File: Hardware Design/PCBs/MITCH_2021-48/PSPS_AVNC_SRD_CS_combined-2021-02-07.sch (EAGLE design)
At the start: 1 part, among them U0-C STM32F411CEUX

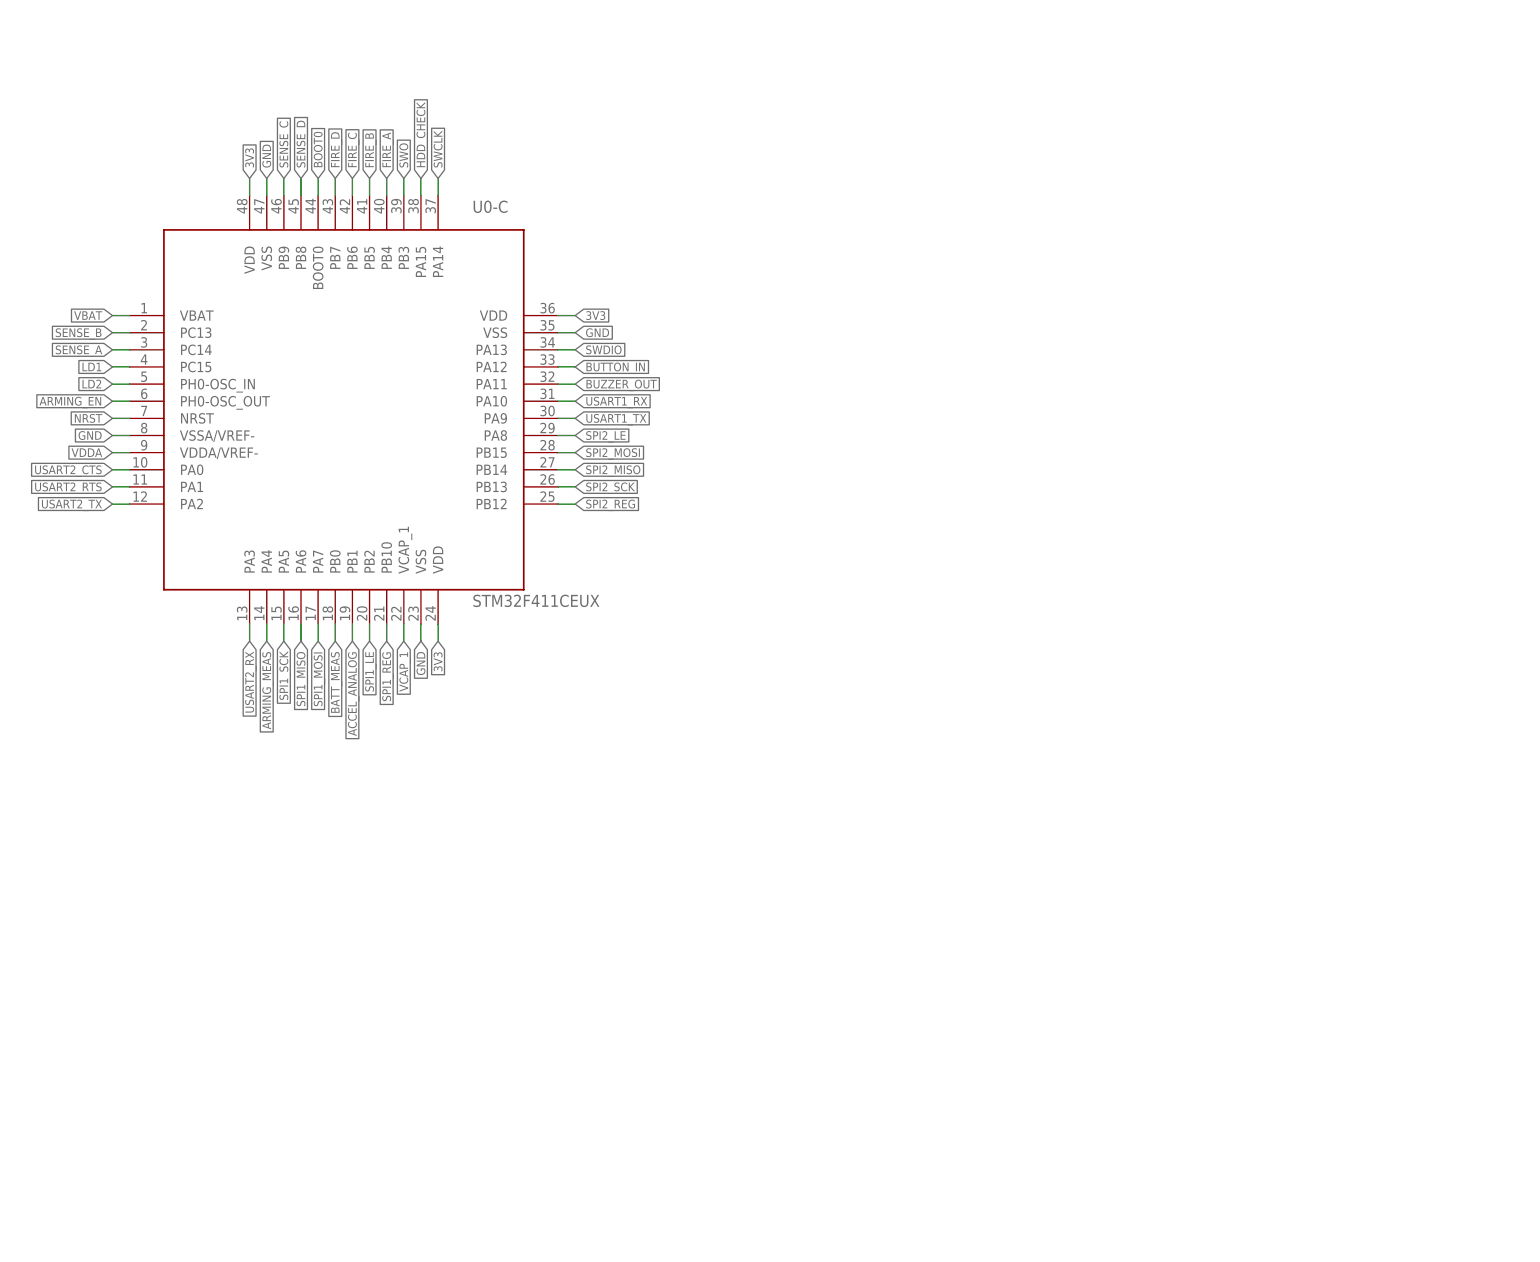
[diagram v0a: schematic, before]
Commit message: Added Shift Registeres, Split Octal Buffers
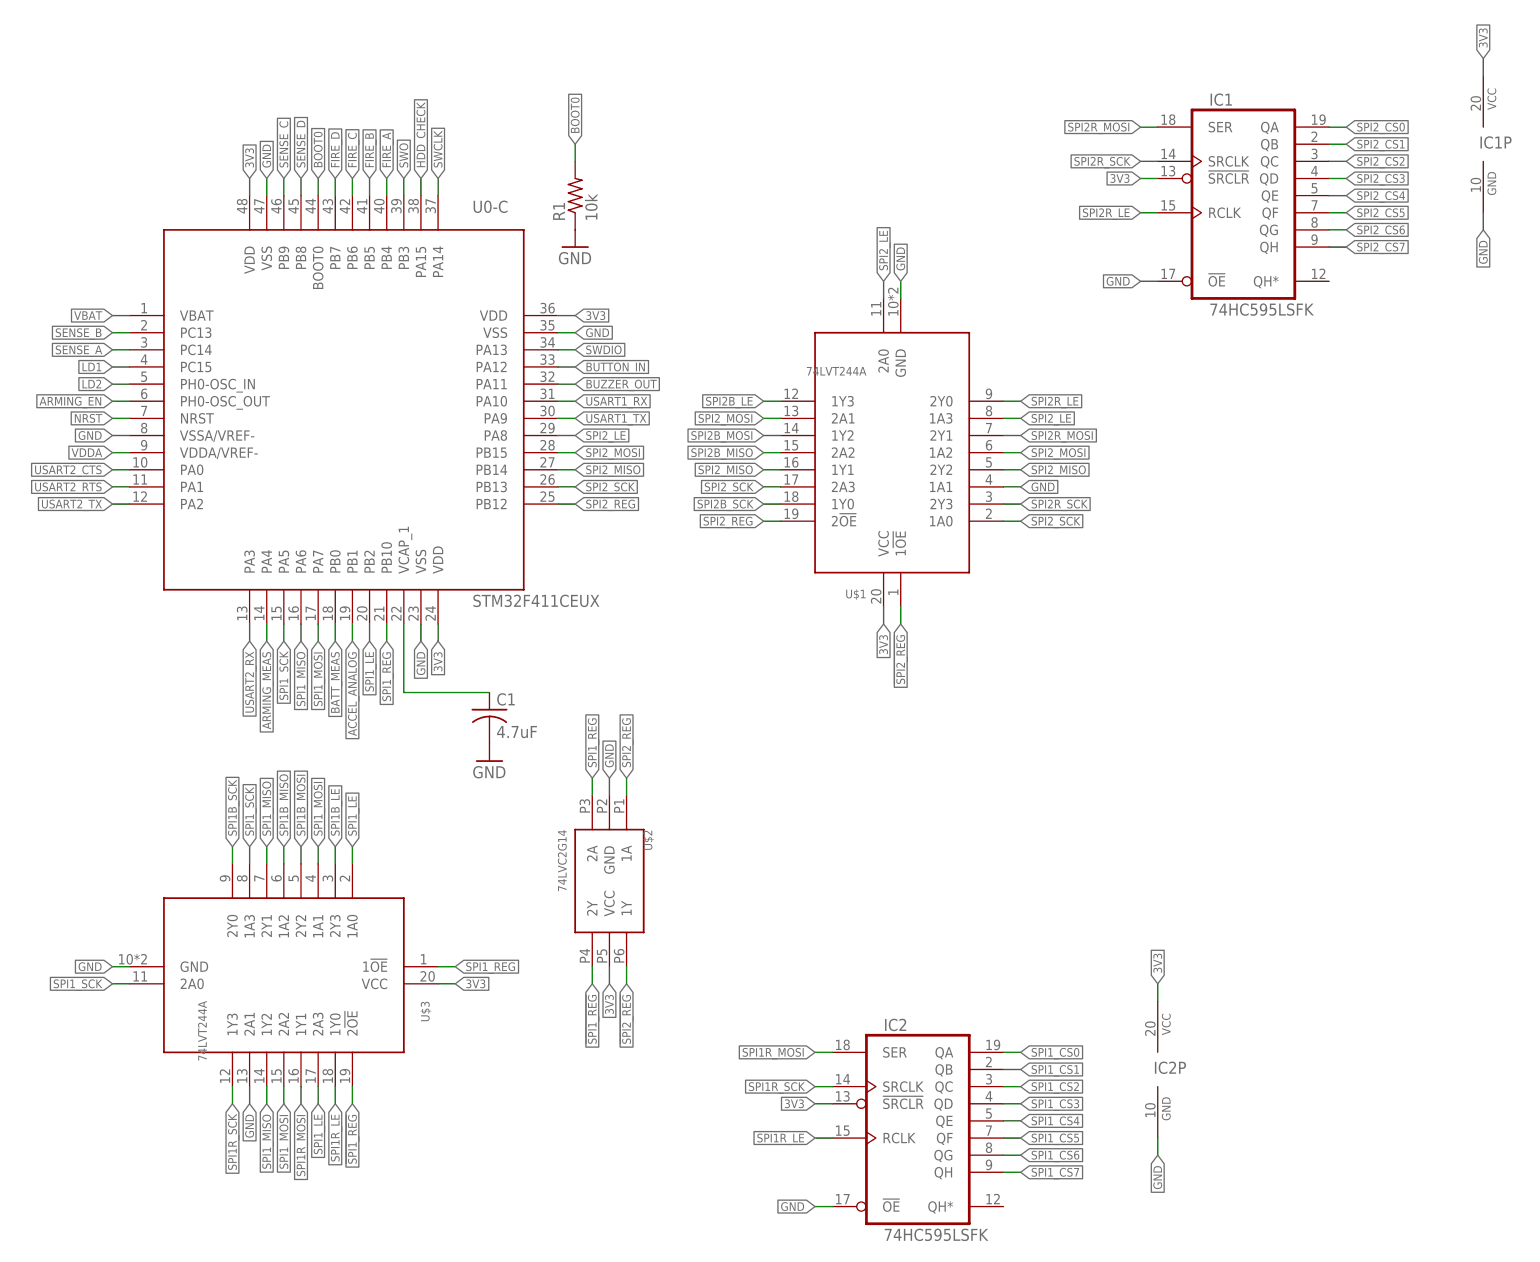
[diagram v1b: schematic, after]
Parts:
- added C1: 4.7uF, resistor:C-USC0805
- added IC1, IC2: 74HC595LSFK, Computer2:74HC595LSFK
- added R1: 10k, resistor:R-US_M0805
- added U$1, U$3: 74LVT244A, Computer2:74LVT244A
- added U$2: 74LVC2G14, Computer2:74LVC2G14
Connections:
- new net !SPI1_REG!: U$2.2Y, U$3.2!OE!
- new net !SPI2_REG!: U$1.1!OE!, U$2.1Y
- new net SPI1B_LE: U$3.2Y3
- new net SPI1B_MISO: U$3.1A2
- new net SPI1B_MOSI: U$3.2Y2
- new net SPI1B_SCK: U$3.2Y0
- new net SPI1R_LE: IC2G$1.RCLK, U$3.1Y0
- new net SPI1R_MOSI: IC2G$1.SER, U$3.1Y1
- new net SPI1R_SCK: IC2G$1.SRCLK, U$3.1Y3
- new net SPI1_CS0: IC2G$1.QA
- new net SPI1_CS1: IC2G$1.QB
- new net SPI1_CS2: IC2G$1.QC
- new net SPI1_CS3: IC2G$1.QD
- new net SPI1_CS4: IC2G$1.QE
- new net SPI1_CS5: IC2G$1.QF
- new net SPI1_CS6: IC2G$1.QG
- new net SPI1_CS7: IC2G$1.QH
- new net SPI2B_LE: U$1.1Y3
- new net SPI2B_MISO: U$1.2A2
- new net SPI2B_MOSI: U$1.1Y2
- new net SPI2B_SCK: U$1.1Y0
- new net SPI2R_LE: IC1G$1.RCLK, U$1.2Y0
- new net SPI2R_MOSI: IC1G$1.SER, U$1.2Y1
- new net SPI2R_SCK: IC1G$1.SRCLK, U$1.2Y3
- new net SPI2_CS0: IC1G$1.QA
- new net SPI2_CS1: IC1G$1.QB
- new net SPI2_CS2: IC1G$1.QC
- new net SPI2_CS3: IC1G$1.QD
- new net SPI2_CS4: IC1G$1.QE
- new net SPI2_CS5: IC1G$1.QF
- new net SPI2_CS6: IC1G$1.QG
- new net SPI2_CS7: IC1G$1.QH
- net 3V3: now also IC1G$1.!SRCLR!, IC1P.VCC, IC2G$1.!SRCLR!, IC2P.VCC, U$1.VCC, U$2.VCC, U$3.VCC
- net BOOT0: now also R1.2
- net GND: now also C1.2, IC1G$1.!OE!, IC1P.GND, IC2G$1.!OE!, IC2P.GND, R1.1, U$1.1A1, U$1.GND, U$2.GND, U$3.2A1, U$3.GND
- net SPI1_LE: now also U$3.1A0, U$3.2A3
- net SPI1_MISO: now also U$3.1Y2, U$3.2Y1
- net SPI1_MOSI: now also U$3.1A1, U$3.2A2
- net SPI1_REG: now also U$2.2A, U$3.1!OE!
- net SPI1_SCK: now also U$3.1A3, U$3.2A0
- net SPI2_LE: now also U$1.1A3, U$1.2A0
- net SPI2_MISO: now also U$1.1Y1, U$1.2Y2
- net SPI2_MOSI: now also U$1.1A2, U$1.2A1
- net SPI2_REG: now also U$1.2!OE!, U$2.1A
- net SPI2_SCK: now also U$1.1A0, U$1.2A3
- net VCAP_1: now also C1.1

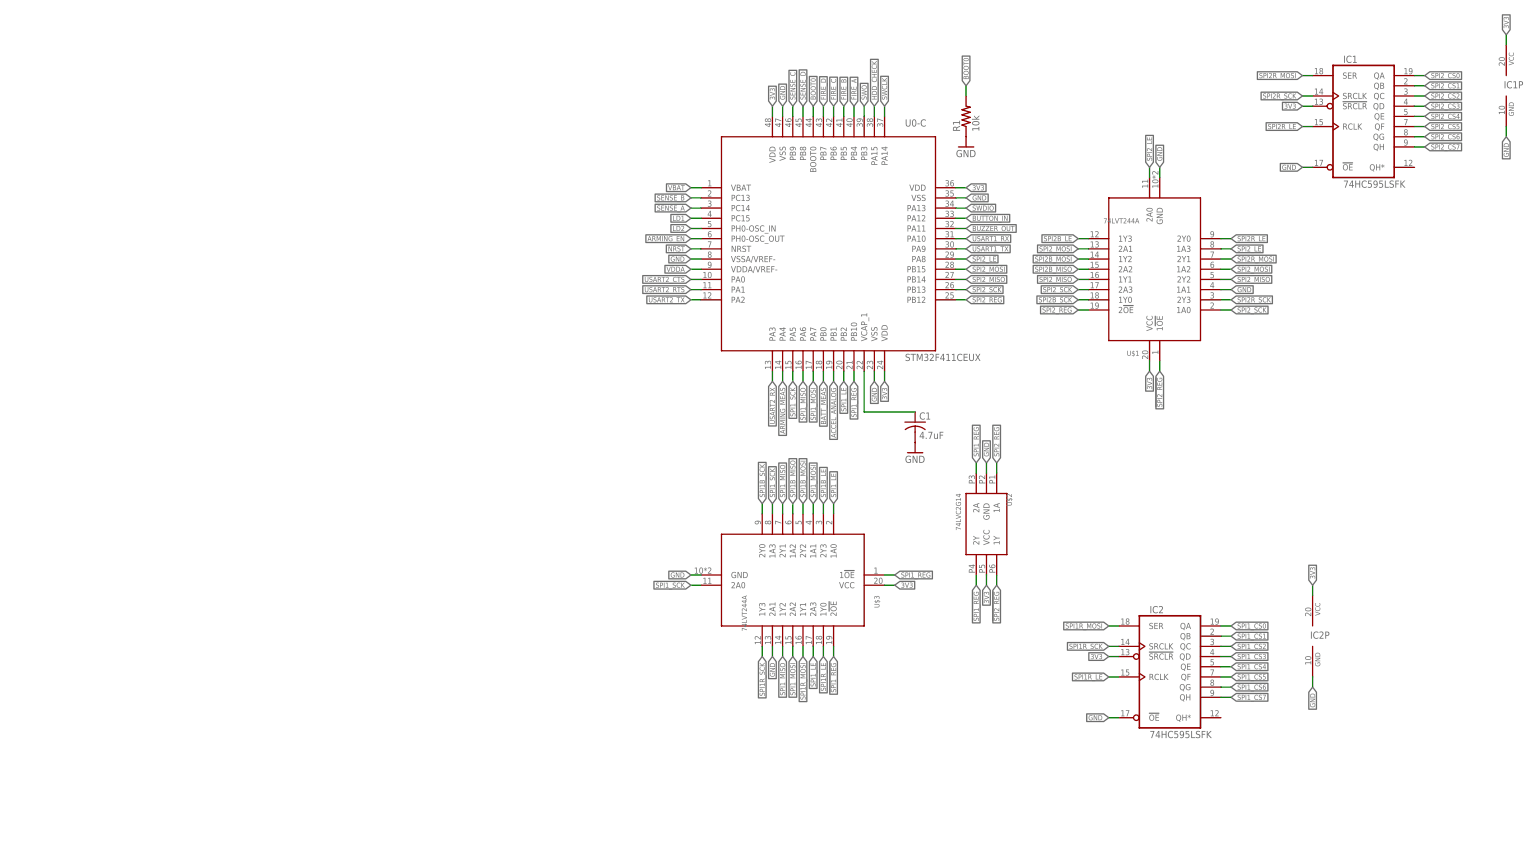
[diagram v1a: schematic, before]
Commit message: Replaces shift registers with dual quad
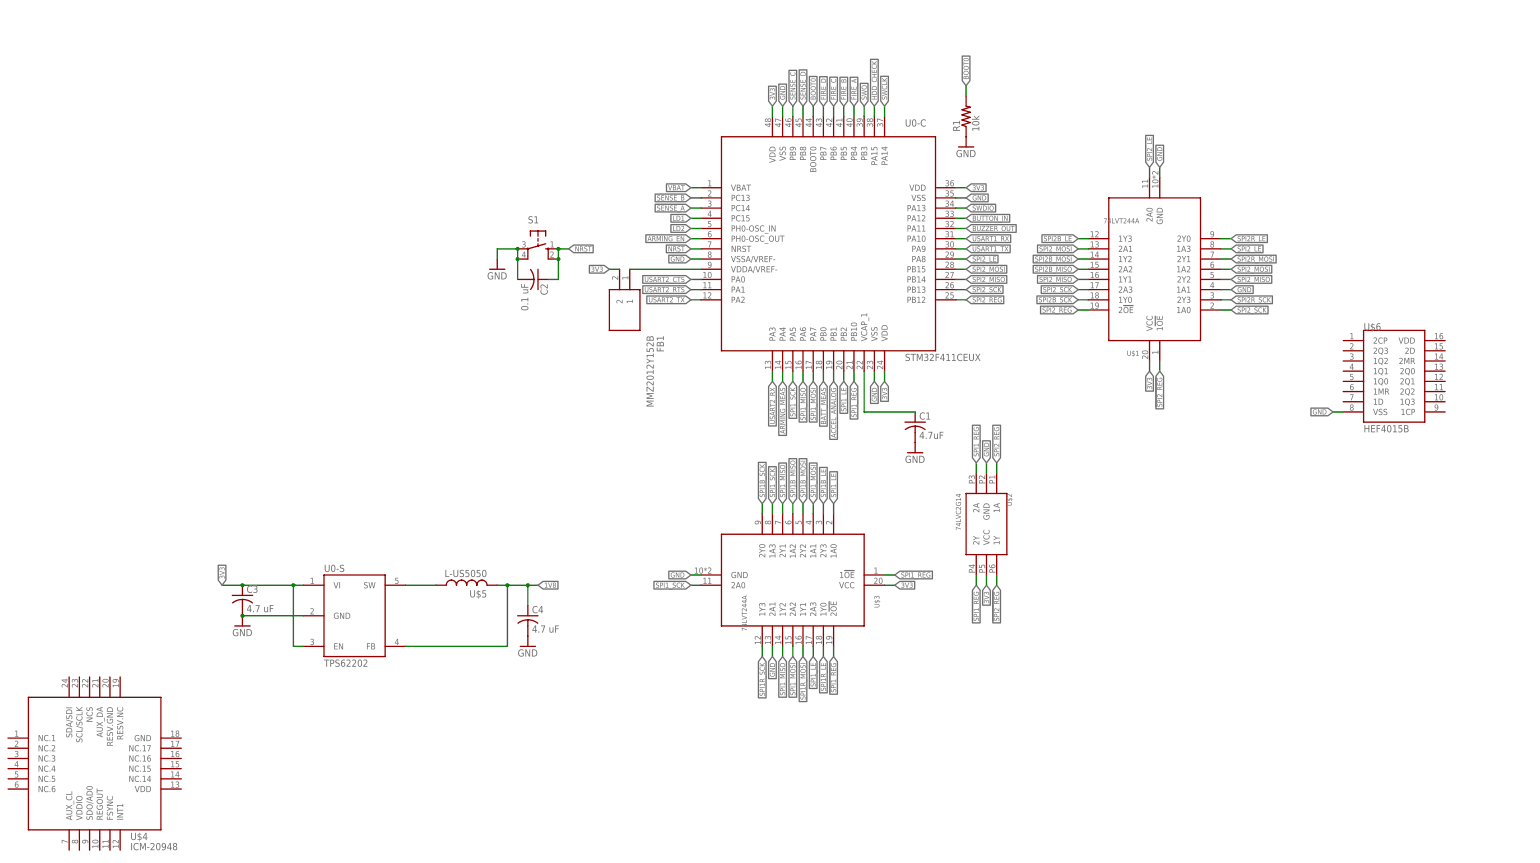
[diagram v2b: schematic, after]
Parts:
- removed IC1, IC2: 74HC595LSFK, Computer2:74HC595LSFK
- added C2: 0.1 uF, resistor:C-USC0805
- added C3, C4: 4.7 uF, resistor:C-USC0805
- added FB1: MMZ2012Y152B, Computer2:MMZ2012Y152B
- added S1: (no value), switch-omron:10-XX
- added U$4: ICM-20948, Computer2:ICM-20948
- added U$5: L-US5050, Computer2:L-US5050
- added U$6: HEF4015B, Computer2:HEF4015B
- added U0-S: TPS62202, Computer2:TPS62202
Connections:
- removed net SPI1_CS0: IC2G$1.QA
- removed net SPI1_CS1: IC2G$1.QB
- removed net SPI1_CS2: IC2G$1.QC
- removed net SPI1_CS3: IC2G$1.QD
- removed net SPI1_CS4: IC2G$1.QE
- removed net SPI1_CS5: IC2G$1.QF
- removed net SPI1_CS6: IC2G$1.QG
- removed net SPI1_CS7: IC2G$1.QH
- removed net SPI2_CS0: IC1G$1.QA
- removed net SPI2_CS1: IC1G$1.QB
- removed net SPI2_CS2: IC1G$1.QC
- removed net SPI2_CS3: IC1G$1.QD
- removed net SPI2_CS4: IC1G$1.QE
- removed net SPI2_CS5: IC1G$1.QF
- removed net SPI2_CS6: IC1G$1.QG
- removed net SPI2_CS7: IC1G$1.QH
- new net 1V8: C4.1, U$5.2, U0-S.FB
- new net U0-S_SW: U$5.1, U0-S.SW
- net 3V3: now also C3.1, FB1.2, U0-S.EN, U0-S.VI; no longer IC1G$1.!SRCLR!, IC1P.VCC, IC2G$1.!SRCLR!, IC2P.VCC
- net GND: now also C2.2, C3.2, C4.2, S1.P, S1.P1, U$6.VSS, U0-S.GND; no longer IC1G$1.!OE!, IC1P.GND, IC2G$1.!OE!, IC2P.GND
- net NRST: now also C2.1, S1.S, S1.S1
- net SPI1R_LE: no longer IC2G$1.RCLK
- net SPI1R_MOSI: no longer IC2G$1.SER
- net SPI1R_SCK: no longer IC2G$1.SRCLK
- net SPI2R_LE: no longer IC1G$1.RCLK
- net SPI2R_MOSI: no longer IC1G$1.SER
- net SPI2R_SCK: no longer IC1G$1.SRCLK
- net VDDA: now also FB1.1

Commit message: Update to PCB
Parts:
- added C5, C6, C7, C8: 0.1 uF, resistor:C-USC0805
- added U$10, U$7, U$8, U$9: SN74LV1T34, Computer2:SN74LV1T34
- added U$11: MS5607, Computer2:MS5607
- added U1-S: ICM-20948, Computer2:ICM-20948
- U$2: value 74LVC2G14 -> 74LVC2G14TSOP; device Computer2:74LVC2G14 -> Computer2:74LVC2G14TSOP
- U$4: value ICM-20948 -> 74ALVC08; device Computer2:ICM-20948 -> Computer2:74ALVC08
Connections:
- new net CS_1V8: U$9G$2.Y, U1-S.NCS
- new net MISO_1V8: U$10G$2.A, U1-S.SDO/AD0
- new net MOSI_1V8: U$7G$2.Y, U1-S.SDA/SDI
- new net SCK_1V8: U$8G$2.Y, U1-S.SCL/SCLK
- new net SPI1_CS0: U$6.1Q0
- new net SPI1_CS1: U$6.1Q1, U$9G$2.A
- new net SPI1_CS2: U$11.CSB@2, U$6.1Q2
- new net SPI1_CS3: U$6.2Q3
- new net SPI2_CS0: U$4.4B, U$6.2Q0
- new net SPI2_CS1: U$4.1B, U$6.2Q1
- new net SPI2_CS2: U$4.2A, U$6.2Q2
- new net SPI2_CS3: U$4.3A, U$6.1Q3
- new net SPI2_SCK0: U$4.4Y
- new net SPI2_SCK1: U$4.1Y
- new net SPI2_SCK2: U$4.2Y
- new net SPI2_SCK3: U$4.3Y
- new net U1-S_REGOUT: C5.1, U1-S.REGOUT
- net 1V8: now also C6.1, C7.1, U$7G$1.VCC, U$8G$1.VCC, U$9G$1.VCC, U1-S.VDD, U1-S.VDDIO
- net 3V3: now also C8.1, U$10G$1.VCC, U$11.VDD, U$4.VCC, U$6.VDD
- net GND: now also C5.2, C6.2, C7.2, C8.2, U$10G$1.GND, U$11.GND, U$11.PS, U$4.GND, U$7G$1.GND, U$8G$1.GND, U$9G$1.GND, U1-S.GND, U1-S.RESV.GND
- net NRST: no longer S1.S
- net SPI1B_MISO: now also U$10G$2.Y, U$11.SDO
- net SPI1B_MOSI: now also U$11.SDI, U$7G$2.A
- net SPI1B_SCK: now also U$11.SCLK, U$8G$2.A
- net SPI1R_LE: now also U$6.1MR
- net SPI1R_MOSI: now also U$6.1D
- net SPI1R_SCK: now also U$6.2CP
- net SPI2R_LE: now also U$6.2MR
- net SPI2R_MOSI: now also U$6.2D
- net SPI2R_SCK: now also U$6.1CP
- net SPI2_SCK: now also U$4.1A, U$4.2B, U$4.3B, U$4.4A
